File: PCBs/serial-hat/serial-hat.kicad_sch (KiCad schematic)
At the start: 11 parts, among them CN1 Modem port, CN2 Printer port, J7 Rpi headers, U2 MAX3232

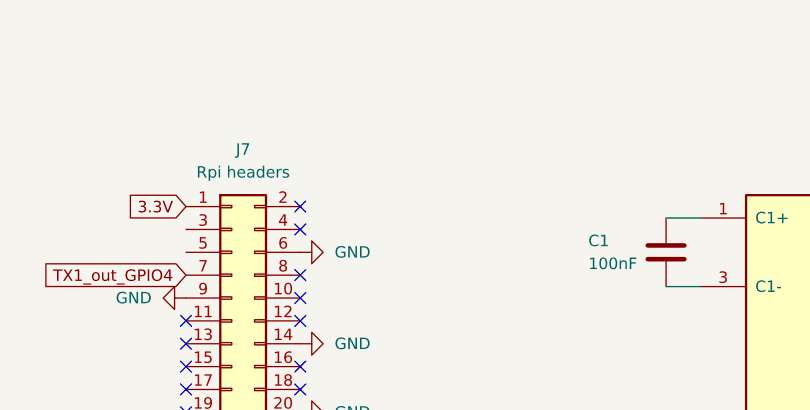
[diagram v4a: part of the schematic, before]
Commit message: Add fan headers
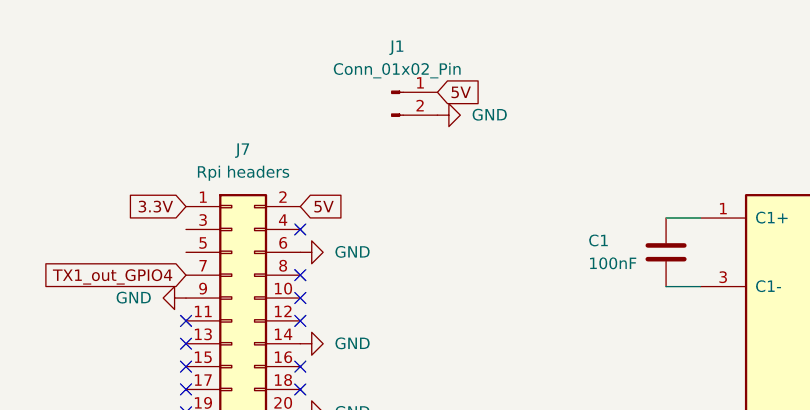
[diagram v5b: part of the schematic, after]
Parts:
- added J1: Conn_01x02_Pin, Connector_PinHeader_2.54mm:PinHeader_1x02_P2.54mm_Vertical, symbol Connector:Conn_01x02_Pin
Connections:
- net GND: now also J1.2 (Pin_2)
- net 5V: now reaches J7.2 (Pin_2)
- net 5V: now also J1.1 (Pin_1)
- no-connect marks 23 -> 22
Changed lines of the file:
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@@
-	)
-	(no_connect
-		(at 50.8 91.44)
 	)
 	(no_connect
@@
 		)
 	)
+	(global_label "5V"
+		(shape input)
+		(at 50.8 91.44 0)
+		(fields_autoplaced yes)
+		(effects
+			(font
+				(size 1.27 1.27)
+			)
+			(justify left)
+		)
+		(property "Intersheetrefs" "${INTERSHEET_REFS}"
+			(at 56.0833 91.44 0)
+			(effects
+				(font
+					(size 1.27 1.27)
+				)
+				(justify left)
+				(hide yes)
+			)
+		)
+	)
 	(global_label "RX1_OUT_GPIO5"
 		(shape input)
@@
 				)
 				(justify right)
+				(hide yes)
+			)
+		)
+	)
+	(global_label "5V"
+		(shape input)
+		(at 66.04 78.74 0)
+		(fields_autoplaced yes)
+		(effects
+			(font
+				(size 1.27 1.27)
+			)
+			(justify left)
+		)
+		(property "Intersheetrefs" "${INTERSHEET_REFS}"
+			(at 71.3233 78.74 0)
+			(effects
+				(font
+					(size 1.27 1.27)
+				)
+				(justify left)
 				(hide yes)
 			)
@@
 					(unit 1)
 				)
+			)
+		)
+	)
+	(symbol
+		(lib_id "power:GND")
+		(at 66.04 81.28 90)
+		(unit 1)
+		(exclude_from_sim no)
+		(in_bom yes)
+		(on_board yes)
+		(dnp no)
+		(fields_autoplaced yes)
+		(property "Reference" "#PWR019"
+			(at 72.39 81.28 0)
+			(effects
+				(font
+					(size 1.27 1.27)
+				)
+				(hide yes)
+			)
+		)
+		(property "Value" "GND"
+			(at 69.85 81.2799 90)
+			(effects
+				(font
+					(size 1.27 1.27)
+				)
+				(justify right)
+			)
+		)
+		(property "Footprint" ""
+			(at 66.04 81.28 0)
+			(effects
+				(font
+					(size 1.27 1.27)
+				)
+				(hide yes)
+			)
+		)
+		(property "Datasheet" ""
+			(at 66.04 81.28 0)
+			(effects
+				(font
+					(size 1.27 1.27)
+				)
+				(hide yes)
+			)
+		)
+		(property "Description" "Power symbol creates a global label with name \"GND\" , ground"
+			(at 66.04 81.28 0)
+			(effects
+				(font
+					(size 1.27 1.27)
+				)
+				(hide yes)
+			)
+		)
+		(pin "1"
+		)
+		(instances
+			(project "serial-hat"
+				(path "/f30a5902-bf77-48c6-ab50-b8e2235ec207"
+					(reference "#PWR019")
+					(unit 1)
+				)
+			)
+		)
+	)
+	(symbol
+		(lib_id "Connector:Conn_01x02_Pin")
+		(at 60.96 78.74 0)
+		(unit 1)
+		(exclude_from_sim no)
+		(in_bom yes)
+		(on_board yes)
+		(dnp no)
+		(fields_autoplaced yes)
+		(property "Reference" "J1"
+			(at 61.595 73.66 0)
+			(effects
+				(font
+					(size 1.27 1.27)
+				)
+			)
+		)
+		(property "Value" "Conn_01x02_Pin"
+			(at 61.595 76.2 0)
+			(effects
+				(font
+					(size 1.27 1.27)
+				)
+			)
+		)
+		(property "Footprint" "Connector_PinHeader_2.54mm:PinHeader_1x02_P2.54mm_Vertical"
+			(at 60.96 78.74 0)
+			(effects
+				(font
+					(size 1.27 1.27)
+				)
+				(hide yes)
+			)
+		)
+		(property "Datasheet" "~"
+			(at 60.96 78.74 0)
+			(effects
+				(font
+					(size 1.27 1.27)
+				)
+				(hide yes)
+			)
+		)
+		(property "Description" "Generic connector, single row, 01x02, script generated"
+			(at 60.96 78.74 0)
+			(effects
+				(font
+					(size 1.27 1.27)
+				)
+				(hide yes)
+			)
+		)
+		(pin "2"
+		)
+		(pin "1"
+		)
+		(instances
+			(project "serial-hat"
+				(path "/f30a5902-bf77-48c6-ab50-b8e2235ec207"
+					(reference "J1")
+					(unit 1)
+				)

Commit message: CISD ready
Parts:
- removed R1, R2: 3.3k, Resistor_SMD:R_0603_1608Metric, symbol Device:R_US
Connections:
- net TX0_in: now also U2.13 (R1IN)
- net TX1_in: now also U2.8 (R2IN)
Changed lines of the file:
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@@
 	(global_label "TX0_in"
 		(shape input)
-		(at 143.51 128.27 0)
-		(fields_autoplaced yes)
-		(effects
-			(font
-				(size 1.27 1.27)
-			)
-			(justify left)
-		)
-		(property "Intersheetrefs" "${INTERSHEET_REFS}"
-			(at 152.6032 128.27 0)
+		(at 135.89 128.27 0)
+		(fields_autoplaced yes)
+		(effects
+			(font
+				(size 1.27 1.27)
+			)
+			(justify left)
+		)
+		(property "Intersheetrefs" "${INTERSHEET_REFS}"
+			(at 144.9832 128.27 0)
 			(effects
 				(font
@@
 	(global_label "TX1_in"
 		(shape input)
-		(at 143.51 133.35 0)
-		(fields_autoplaced yes)
-		(effects
-			(font
-				(size 1.27 1.27)
-			)
-			(justify left)
-		)
-		(property "Intersheetrefs" "${INTERSHEET_REFS}"
-			(at 152.6032 133.35 0)
-			(effects
-				(font
-					(size 1.27 1.27)
-				)
-				(justify left)
-				(hide yes)
-			)
-		)
-	)
-	(symbol
-		(lib_id "Device:R_US")
-		(at 139.7 128.27 90)
-		(unit 1)
-		(exclude_from_sim no)
-		(in_bom yes)
-		(on_board yes)
-		(dnp no)
-		(property "Reference" "R1"
-			(at 137.922 126.238 90)
-			(effects
-				(font
-					(size 1.27 1.27)
-				)
-			)
-		)
-		(property "Value" "3.3k"
-			(at 142.748 126.238 90)
-			(effects
-				(font
-					(size 1.27 1.27)
-				)
-			)
-		)
-		(property "Footprint" "Resistor_SMD:R_0603_1608Metric"
-			(at 139.954 127.254 90)
-			(effects
-				(font
-					(size 1.27 1.27)
-				)
-				(hide yes)
-			)
-		)
-		(property "Datasheet" "~"
-			(at 139.7 128.27 0)
-			(effects
-				(font
-					(size 1.27 1.27)
-				)
-				(hide yes)
-			)
-		)
-		(property "Description" "Resistor, US symbol"
-			(at 139.7 128.27 0)
-			(effects
-				(font
-					(size 1.27 1.27)
-				)
-				(hide yes)
-			)
-		)
-		(property "LCSC" "C21190"
-			(at 139.7 128.27 90)
-			(effects
-				(font
-					(size 1.27 1.27)
-				)
-				(hide yes)
-			)
-		)
-		(pin "2"
-		)
-		(pin "1"
-		)
-		(instances
-			(project "serial-hat"
-				(path "/f30a5902-bf77-48c6-ab50-b8e2235ec207"
-					(reference "R1")
-					(unit 1)
-				)
+		(at 135.89 133.35 0)
+		(fields_autoplaced yes)
+		(effects
+			(font
+				(size 1.27 1.27)
+			)
+			(justify left)
+		)
+		(property "Intersheetrefs" "${INTERSHEET_REFS}"
+			(at 144.9832 133.35 0)
+			(effects
+				(font
+					(size 1.27 1.27)
+				)
+				(justify left)
+				(hide yes)
 			)
 		)
@@
 					(unit 1)
 				)
-			)
-		)
-	)
-	(symbol
-		(lib_id "Device:R_US")
-		(at 139.7 133.35 90)
-		(unit 1)
-		(exclude_from_sim no)
-		(in_bom yes)
-		(on_board yes)
-		(dnp no)
-		(property "Reference" "R2"
-			(at 137.922 131.318 90)
-			(effects
-				(font
-					(size 1.27 1.27)
-				)
-			)
-		)
-		(property "Value" "3.3k"
-			(at 142.748 131.318 90)
-			(effects
-				(font
-					(size 1.27 1.27)
-				)
-			)
-		)
-		(property "Footprint" "Resistor_SMD:R_0603_1608Metric"
-			(at 139.954 132.334 90)
-			(effects
-				(font
-					(size 1.27 1.27)
-				)
-				(hide yes)
-			)
-		)
-		(property "Datasheet" "~"
-			(at 139.7 133.35 0)
-			(effects
-				(font
-					(size 1.27 1.27)
-				)
-				(hide yes)
-			)
-		)
-		(property "Description" "Resistor, US symbol"
-			(at 139.7 133.35 0)
-			(effects
-				(font
-					(size 1.27 1.27)
-				)
-				(hide yes)
-			)
-		)
-		(property "LCSC" "C21190"
-			(at 139.7 133.35 90)
-			(effects
-				(font
-					(size 1.27 1.27)
-				)
-				(hide yes)
-			)
-		)
-		(pin "2"
-		)
-		(pin "1"
-		)
-		(instances
-			(project "serial-hat"
-				(path "/f30a5902-bf77-48c6-ab50-b8e2235ec207"
-					(reference "R2")
-					(unit 1)
-				)

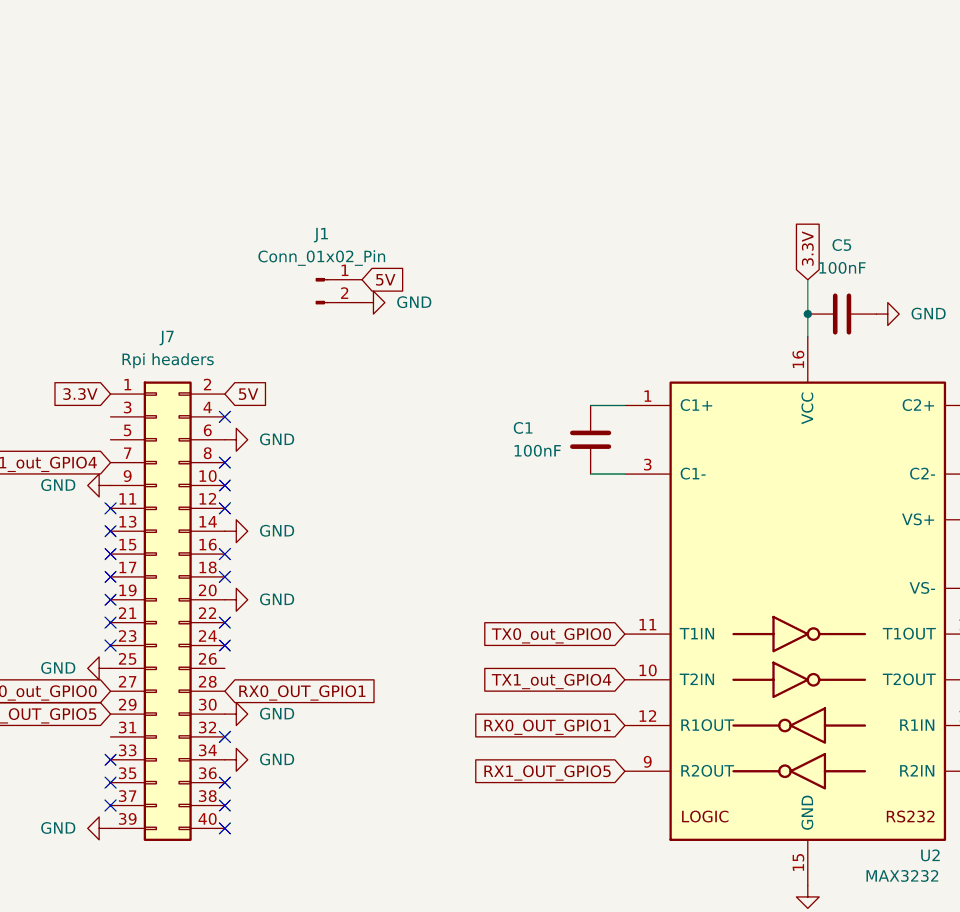
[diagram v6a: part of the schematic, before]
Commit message: Add gpio-fan ability
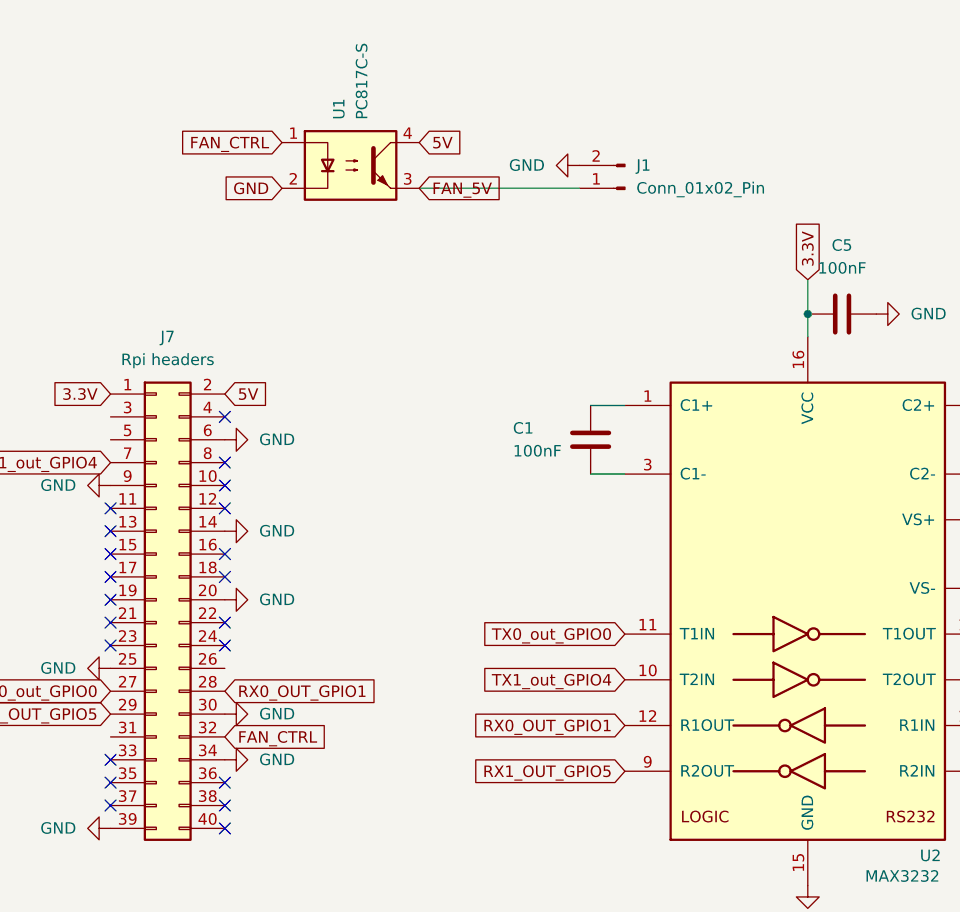
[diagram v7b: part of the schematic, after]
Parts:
- added U1: PC817C-S, Package_SO:SOP-4_3.8x4.1mm_P2.54mm, symbol Isolator:PC817
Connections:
- net 5V: now also U1.4; no longer J1.1 (Pin_1)
- net GND: now also U1.2
- net FAN_CTRL: now reaches J7.32 (Pin_32)
- net FAN_CTRL: now also U1.1
- new net FAN_5V: J1.1 (Pin_1), U1.3
- no-connect marks 22 -> 21

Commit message: Update to new lib
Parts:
- CN1, CN2: footprint DIN5:CONN-TH_DIN-504-M10 -> Colins-Kicad:DIN-5-M C2939346; symbol DIN:DIN-504 -> Colins-Kicad:DIN-5_180degree
- U1: footprint Package_SO:SOP-4_3.8x4.1mm_P2.54mm -> Colins-Kicad:PC817C-S C3008369
